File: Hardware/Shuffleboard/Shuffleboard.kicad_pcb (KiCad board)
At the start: 4 copper layers, 130 x 131.5 mm, 70 parts, among them IC1 DG3157EDL-T1-GE3, IC2 DG3157EDL-T1-GE3, J1 1869279, J2 1869279, Q1 NMOS, U1 COM-09032, U2 PAM8302AAS, U3 LMV331, U4 INND-TS56RCB, U5 INND-TS56RCB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

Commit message: Finished screen
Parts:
- moved J2 20.6 mm to (120.5, 73.0)
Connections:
- J2 pad 4: unconnected-(J2-Pad4) -> /PB7_MISO
- J2 pad 5: unconnected-(J2-Pad5) -> /PB6_CS
- J2 pad 6: unconnected-(J2-Pad6) -> /PA13_DC
- J2 pad 7: unconnected-(J2-Pad7) -> /PB15_RESET
- J2 pad 8: unconnected-(J2-Pad8) -> GND
- U7 pad 1: unconnected-(U7-GND-Pad1) -> GND
- U7 pad 10: unconnected-(U7-LITE-Pad10) -> +3.3V
- U7 pad 2: unconnected-(U7-VCC-Pad2) -> +3.3V
- U7 pad 3: unconnected-(U7-RESET-Pad3) -> /PB15_RESET
- U7 pad 4: unconnected-(U7-D/C-Pad4) -> /PA13_DC
- U7 pad 6: unconnected-(U7-TFT_CS-Pad6) -> /PB6_CS
- U7 pad 7: unconnected-(U7-MOSI-Pad7) -> /PB8_MOSI
- U7 pad 8: unconnected-(U7-SCK-Pad8) -> /PB9_SPI_CLK
- U7 pad 9: unconnected-(U7-MISO-Pad9) -> /PB7_MISO
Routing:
- net /PB16_L/P: track 51.5 -> 73.2 mm
- net /PB9_SPI_CLK: track 54.9 -> 74.7 mm
- net /PB8_MOSI: track 64.8 -> 83.8 mm

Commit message: finished layout
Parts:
- added G***: LOGO, Footprint:longhorns, B.Cu at (174.2, 106.4)
- C1, C3, C4, C5, C6, C7, C8: value 100n -> ~
- C10, C11: value 100n -> ~; moved to F.Cu
- C2: value 4.7u -> ~
- C9: value 1u -> ~
- D1: value Red -> ~
- D32: value Green -> ~
- F1: value 1A -> ~
- H1, H2, H3, H4, H5, H6: value MountingHole -> ~
- IC1, IC2: value DG3157EDL-T1-GE3 -> ~
- J1, J2: value 1869279 -> TBJ05-08-1-G-G; footprint Footprint:1869279 -> ShuffleboardFootprints:TBJ05081GG
- LS1: value CMS-3012-18T -> ~
- Q1: value NMOS -> ~
- R1, R12, R45, R5, R9: value 10k -> ~; footprint Resistor_SMD:R_0603_1608Metric_Pad0.98x0.95mm_HandSolder -> Resistor_THT:R_Axial_DIN0207_L6.3mm_D2.5mm_P7.62mm_Horizontal
- R10, R14: value 330 -> ~
- R11, R2, R3, R4, R6, R7, R8: value 1k -> ~; footprint Resistor_SMD:R_0603_1608Metric_Pad0.98x0.95mm_HandSolder -> Resistor_THT:R_Axial_DIN0207_L6.3mm_D2.5mm_P7.62mm_Horizontal
- R13: value 100k -> ~
- R15, R16, R17, R18, R19, R20, R21, R22, R23, R24, R25, R26, R27, R28, R29, R30: value 100 -> ~
- RV1: value R_Potentiometer -> ~
- S1, S2: value TL3301FF160QG -> ~
- TP1: value GND -> ~
- TP2: value +3.3 -> ~
- U1: value COM-09032 -> ~
- U2: value PAM8302AAS -> ~
- U3: value LMV331 -> ~
- U4, U5: value INND-TS56RCB -> ~
- U6, U8: value LOGIC-74HC595N_DIP16_ -> ~; moved to F.Cu
- U7: value Adafruit ST7735R -> ~
- moved U7 126.9 mm to (175.4, 55.9)
- moved J2 35.1 mm to (120.0, 37.9), turned to -90 degrees
- moved U6 30.2 mm to (147.5, 42.5), turned to 0 degrees
- moved U8 28.1 mm to (203.7, 42.4)
- moved R12 27.3 mm to (155.5, 121.4), turned to 90 degrees
- moved C11 26.3 mm to (198.5, 46.0), turned to -90 degrees
- moved R9 25.8 mm to (153.4, 89.0)
- moved R45 25.7 mm to (141.9, 89.0)
- moved R7 19.2 mm to (196.5, 123.1), turned to 90 degrees
- moved R15 19.0 mm to (138.5, 41.9)
- moved R16 19.0 mm to (141.0, 41.9)
- moved R17 19.0 mm to (138.5, 50.8)
- moved R18 19.0 mm to (133.5, 50.9)
- moved R19 19.0 mm to (131.0, 50.9)
- moved R20 19.0 mm to (133.5, 41.9)
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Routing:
- net /PB7_MISO: track 0.00 -> 75.9 mm
- net /PB9_SPI_CLK: track 74.7 -> 142.5 mm, vias 3 -> 1
- net /PB6_CS: track 0.00 -> 66.2 mm
- net /PA13_DC: track 0.00 -> 59.0 mm
- net /PB15_RESET: track 0.00 -> 54.4 mm
- net /7Seg/QH1: track 8.92 -> 51.9 mm
- net /DACOut: track 81.5 -> 109.3 mm, vias 1 -> 0
- net /PB16_L/P: track 73.2 -> 95.0 mm, vias 1 -> 3
- net Net-(U6-QE): track 38.3 -> 17.1 mm, vias 2 -> 1
- net /Connector/HOR_PB18_ADC1_5: track 93.8 -> 114.0 mm
- net Net-(U6-QB): track 23.3 -> 6.57 mm, vias 0 -> 1
- net Net-(U6-QF): track 29.3 -> 13.1 mm, vias 0 -> 1
- net Net-(U8-QG): track 20.7 -> 4.58 mm, vias 2 -> 1
- net Net-(U6-QH): track 22.2 -> 6.13 mm, vias 2 -> 1
- net /Connector/VER_PB19_ADC1_6: track 81.1 -> 97.1 mm
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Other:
- board size 130 x 131.5 mm -> 130 x 131.2 mm
- board text added: "Rishi Bala Anh-Vu Nguyen ECE319H"
- board text removed: "Rishi Bala Anh-Vu Nguyen"

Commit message: finalized
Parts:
- added C12: 100n, Capacitor_SMD:C_0603_1608Metric_Pad1.08x0.95mm_HandSolder, F.Cu at (196.2, 111.5)
- C11: value ~ -> 100n
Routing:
- net GND: track 86.7 -> 91.3 mm
- net +3.3V: track 65.0 -> 68.4 mm
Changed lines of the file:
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@@
 			)
 		)
-		(property "Value" "~"
+		(property "Value" "100n"
 			(at 0 1.43 90)
 			(layer "F.Fab")
@@
 		)
 	)
+	(footprint "Capacitor_SMD:C_0603_1608Metric_Pad1.08x0.95mm_HandSolder"
+		(layer "F.Cu")
+		(at 196.175 111.505)
+		(descr "Capacitor SMD 0603 (1608 Metric), square (rectangular) end terminal, IPC-7351 nominal with elongated pad for handsoldering. (Body size source: IPC-SM-782 page 76, https://www.pcb-3d.com/wordpress/wp-content/uploads/ipc-sm-782a_amendment_1_and_2.pdf)")
+		(tags "capacitor handsolder")
+		(property "Reference" "C12"
+			(at 0 -1.43 0)
+			(layer "F.SilkS")
+			(hide yes)
+			(effects
+				(font
+					(size 1 1)
+					(thickness 0.15)
+				)
+			)
+		)
+		(property "Value" "100n"
+			(at 0 1.43 0)
+			(layer "F.Fab")
+			(hide yes)
+			(effects
+				(font
+					(size 1 1)
+					(thickness 0.15)
+				)
+			)
+		)
+		(property "Datasheet" "https://datasheets.kyocera-avx.com/AutoMLCCKAM.pdf"
+			(at 0 0 0)
+			(layer "F.Fab")
+			(hide yes)
+			(effects
+				(font
+					(size 1.27 1.27)
+				)
+			)
+		)
+		(property "Description" "Unpolarized capacitor"
+			(at 0 0 0)
+			(layer "F.Fab")
+			(hide yes)
+			(effects
+				(font
+					(size 1.27 1.27)
+				)
+			)
+		)
+		(property "KiLib_Generator" "SMD_2terminal_chip_molded"
+			(at 0 0 0)
+			(layer "F.SilkS")
+			(hide yes)
+			(effects
+				(font
+					(size 1 1)
+					(thickness 0.15)
+				)
+			)
+		)
+		(property "Mouser Link" "https://www.mouser.com/ProductDetail/KYOCERA-AVX/06031C104K4T2A?qs=7MVldsJ5UaycASOsZ6%2FbJQ%3D%3D"
+			(at 0 0 0)
+			(unlocked yes)
+			(layer "F.Fab")
+			(hide yes)
+			(effects
+				(font
+					(size 1 1)
+					(thickness 0.15)
+				)
+			)
+		)
+		(property "JLCPCB #" "C1880996"
+			(at 0 0 0)
+			(unlocked yes)
+			(layer "F.Fab")
+			(hide yes)
+			(effects
+				(font
+					(size 1 1)
+					(thickness 0.15)
+				)
+			)
+		)
+		(property "Mouser Part Number" "581-06031C104K4T2A"
+			(at 0 0 0)
+			(unlocked yes)
+			(layer "F.Fab")
+			(hide yes)
+			(effects
+				(font
+					(size 1 1)
+					(thickness 0.15)
+				)
+			)
+		)
+		(property ki_fp_filters "C_*")
+		(sheetname "/Speaker/")
+		(sheetfile "speaker.kicad_sch")
+		(units
+			(unit
+				(name "A")
+				(pins "1" "2")
+			)
+		)
+		(attr smd)
+		(duplicate_pad_numbers_are_jumpers no)
+		(fp_line
+			(start -0.146267 -0.51)
+			(end 0.146267 -0.51)
+			(stroke
+				(width 0.12)
+				(type solid)
+			)
+			(layer "F.SilkS")
+		)
+		(fp_line
+			(start -0.146267 0.51)
+			(end 0.146267 0.51)
+			(stroke
+				(width 0.12)
+				(type solid)
+			)
+			(layer "F.SilkS")
+		)
+		(fp_rect
+			(start -1.65 -0.73)
+			(end 1.65 0.73)
+			(stroke
+				(width 0.05)
+				(type solid)
+			)
+			(fill no)
+			(layer "F.CrtYd")
+		)
+		(fp_rect
+			(start -0.8 -0.4)
+			(end 0.8 0.4)
+			(stroke
+				(width 0.1)
+				(type solid)
+			)
+			(fill no)
+			(layer "F.Fab")
+		)
+		(fp_text user "${REFERENCE}"
+			(at 0 0 0)
+			(layer "F.Fab")
+			(effects
+				(font
+					(size 0.4 0.4)
+					(thickness 0.06)
+				)
+			)
+		)
+		(pad "1" smd roundrect
+			(at -0.8625 0)
+			(size 1.075 0.95)
+			(layers "F.Cu" "F.Mask" "F.Paste")
+			(roundrect_rratio 0.25)
+			(net "+3.3V")
+			(pintype "passive")
+		)
+		(pad "2" smd roundrect
+			(at 0.8625 0)
+			(size 1.075 0.95)
+			(layers "F.Cu" "F.Mask" "F.Paste")
+			(roundrect_rratio 0.25)
+			(net "GND")
+			(pintype "passive")
+		)
+		(embedded_fonts no)
+		(model "${KICAD10_3DMODEL_DIR}/Capacitor_SMD.3dshapes/C_0603_1608Metric.step"
+			(offset
+				(xyz 0 0 0)
+			)
+			(scale
+				(xyz 1 1 1)
+			)
+			(rotate
+				(xyz 0 0 0)
+			)
+		)
+	)
 	(footprint "TestPoint:TestPoint_THTPad_1.5x1.5mm_Drill0.7mm"
 		(layer "F.Cu")
@@
 	)
 	(segment
+		(start 197.0375 111.505)
+		(end 196.2625 112.28)
+		(width 0.2)
+		(layer "F.Cu")
+		(net "GND")
+	)
+	(segment
 		(start 168.22 98.28)
 		(end 168.5 98)
@@
 	)
 	(segment
+		(start 196.2625 112.28)
+		(end 193.8925 112.28)
+		(width 0.2)
+		(layer "F.Cu")
+		(net "GND")
+	)
+	(segment
 		(start 122.18 112.3875)
 		(end 124.25 110.3175)
@@
 	)
 	(segment
+		(start 193.8925 112.28)
+		(end 193.1125 111.5)
+		(width 0.2)
+		(layer "F.Cu")
+		(net "GND")
+	)
+	(segment
 		(start 187.75 101.41)
 		(end 189.91 101.41)
@@
 	)
 	(segment
+		(start 195.25 108.135)
+		(end 195.25 108.5)
+		(width 0.2)
+		(layer "F.Cu")
+		(net "+3.3V")
+	)
+	(segment
 		(start 162.54 103.25)
 		(end 162.54 102.04)
@@
 	)
 	(segment
+		(start 195.25 108.135)
+		(end 194.613106 108.135)
+		(width 0.2)
+		(layer "F.Cu")
+		(net "+3.3V")
+	)
+	(segment
 		(start 155.5 121.37)
 		(end 153.63 121.37)
@@
 	(segment
 		(start 197.125 108.135)
-		(end 194.613106 108.135)
+		(end 195.25 108.135)
 		(width 0.2)
 		(layer "F.Cu")
@@
 	)
 	(segment
+		(start 195.3125 108.5625)
+		(end 195.3125 111.505)
+		(width 0.2)
+		(layer "F.Cu")
+		(net "+3.3V")
+	)
+	(segment
 		(start 226.5 30.25)
 		(end 228.5 28.25)
 		(width 0.2)
 		(layer "F.Cu")
+		(net "+3.3V")
+	)
+	(segment
+		(start 195.25 108.5)
+		(end 195.3125 108.5625)
+		(width 0.2)
+		(layer "F.Cu")

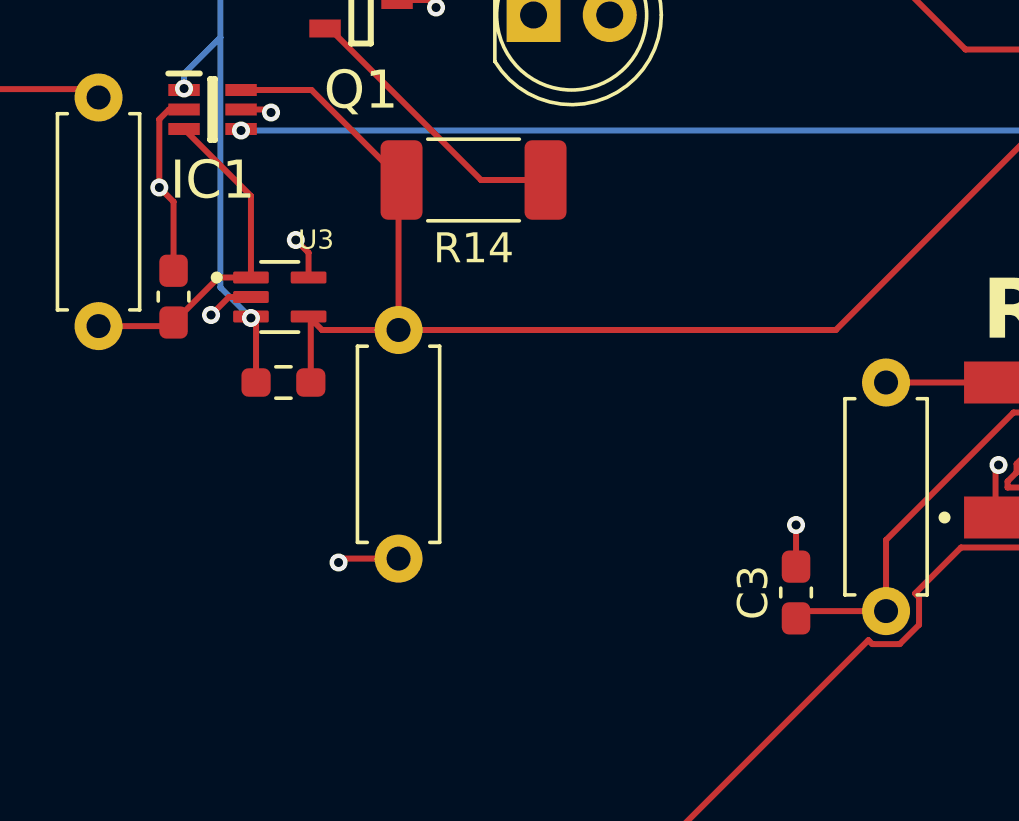
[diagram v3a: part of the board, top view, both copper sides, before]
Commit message: tht resistors
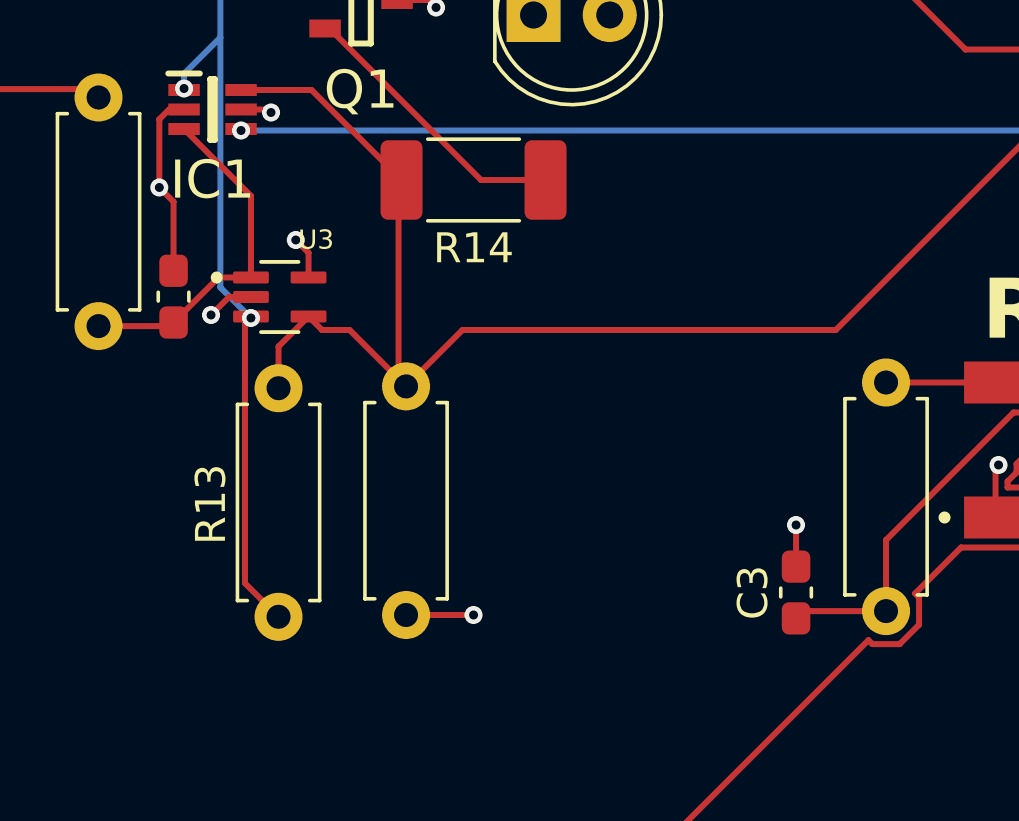
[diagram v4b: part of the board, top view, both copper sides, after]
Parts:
- C1, C10, C2, C3, C4, C5, C6, C7, C8: value ~ -> 100n
- C9: value ~ -> 1u
- D1: value ~ -> Red
- D32: value ~ -> Green
- R1, R12, R45, R5, R9: value ~ -> 10k
- R10, R14: value ~ -> 330
- R11, R2, R3, R4, R6, R7, R8: value ~ -> 1k
- R13: value ~ -> 10k; footprint Resistor_SMD:R_0603_1608Metric_Pad0.98x0.95mm_HandSolder -> Resistor_THT:R_Axial_DIN0207_L6.3mm_D2.5mm_P7.62mm_Horizontal
- R15, R16, R17, R18, R19, R20, R21, R22, R23, R24, R25, R26, R27, R28, R29, R30: value ~ -> 100
- U3: value ~ -> Comparator
- moved R13 7.81 mm to (151.5, 123.3), turned to 90 degrees
- moved R12 1.90 mm to (155.8, 123.2)
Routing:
- net /Inputs/Vref: track 33.1 -> 41.6 mm
- net /Inputs/CompOut: track 46.8 -> 51.0 mm

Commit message: sent to jlc
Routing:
- net /PB9_SPI_CLK: track 142.5 -> 146.2 mm
- net +3.3V: track 68.6 -> 65.3 mm, vias 17 -> 18
- net Net-(U6-QD): track 18.2 -> 20.2 mm
- net Net-(U6-QB): track 6.57 -> 8.24 mm
- net Net-(U8-QE): track 8.79 -> 10.4 mm
- net /PB8_MOSI: track 87.7 -> 89.0 mm
- net /Inputs/Vref: track 41.6 -> 42.7 mm
- net GND: track 91.3 -> 92.4 mm
- net Net-(U8-QH): track 18.3 -> 19.2 mm
- net Net-(U8-QD): track 8.26 -> 9.19 mm
- net Net-(U8-QB): track 15.2 -> 15.9 mm
- net Net-(U8-QA): track 17.6 -> 18.3 mm
